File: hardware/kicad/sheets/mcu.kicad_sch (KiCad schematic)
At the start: 44 parts, among them J1 USB-C, J14 QWIIC, J5 DISPLAY, J6 NAV_SW, J7 AUX, SW1 RESET, SW2 BOOT, U1 ESP32-S3-WROOM-1U-N16R2, U4 SRV05-4

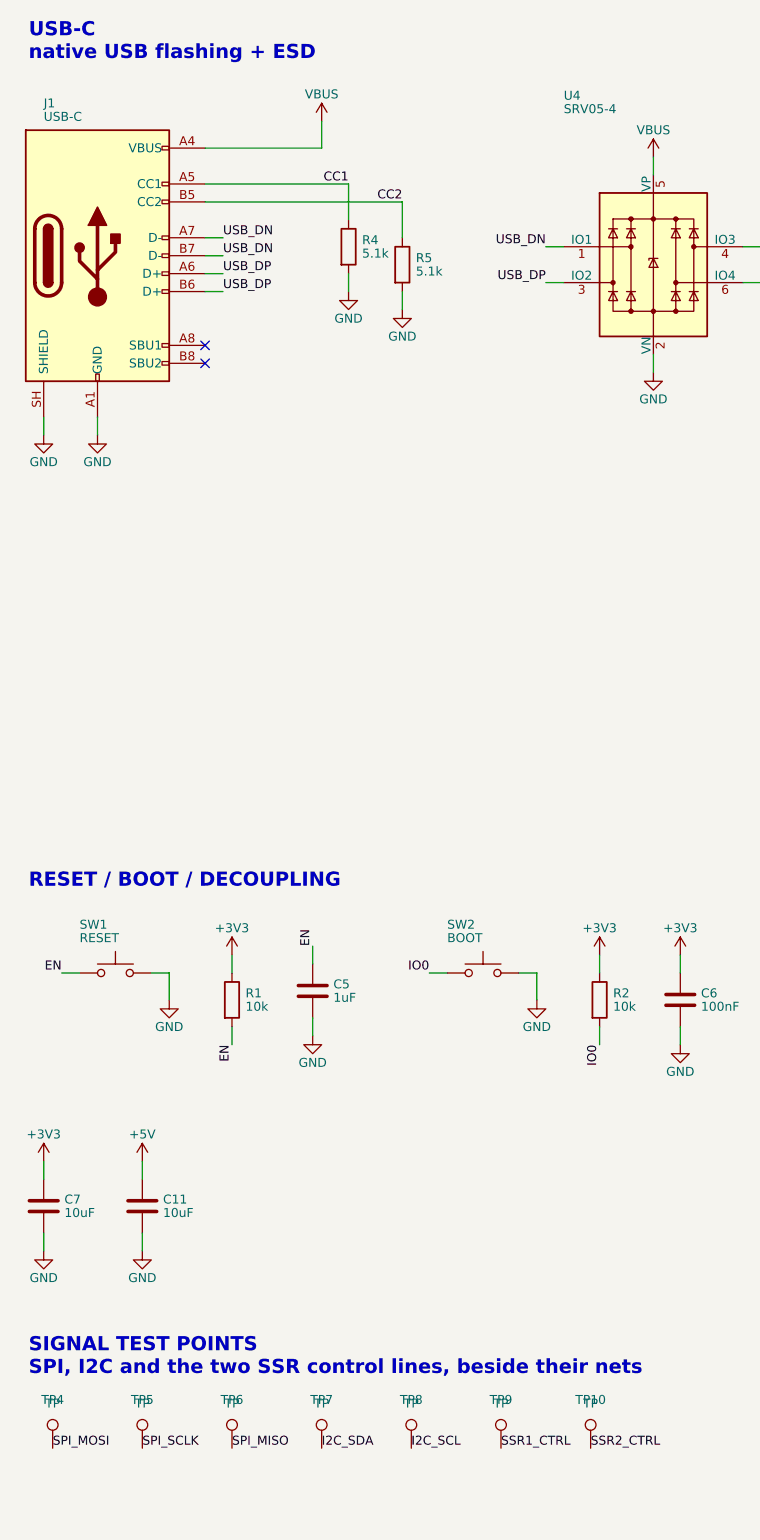
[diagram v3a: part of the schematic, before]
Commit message: hardware: flags at their sources, tri-state MAX31856, Q4 flipped, make erc
Second batch from SCHEMATIC-REVIEW-2026-10-22.md (findings 5, 7, 14, 15,
16 and the local half of 19).

PWR_FLAGs: the power sheet's parked corner is gone. Each flag now sits
where its rail is created - J2.1 (VIN), J2.2 (GND), Q8 source (VIN_P),
L1 output (BUCK_5V) and J1 pin A4 (VBUS, on the mcu sheet) - with the
value text shown on all of them.

MAX31856: U3 and U5 now use bisque:MAX31856 from the new project library
bisque.kicad_sym (registered in sym-lib-table), a copy of the KiCad
symbol with SDO typed tri-state, which is what the part does while CS is
high. The ERC exclusion that papered over the shared SPI_MISO is removed;
ERC is clean with no exclusions.

Q4 is mirrored so the high-side P-FET reads source-up to +5V and drain
down to SSR_EN. One Value string per LCSC part (C38/C44/C45 22uF/25V,
R11 100R 1%); C46 moved 5 mm right to clear the longer text. Every test
point's Value is its net name (TP1 "+3V3" ... TP12 "WDT_CT_P"), so the
board's Value fields, the JLC BOM and the schematic PDF regenerate.

make erc runs kicad-cli ERC at every severity and fails on any
violation; lib_symbol_mismatch, endpoint_off_grid and
same_local_global_label are promoted to errors in the project. It is not
part of pcb-check or CI on purpose.

Board: sync changed only Value fields (0 re-netted); gerbers differ by
timestamp only; DRC 0; full make pcb-check passes.

Co-Authored-By: Claude Fable 5.1 <noreply@anthropic.com>
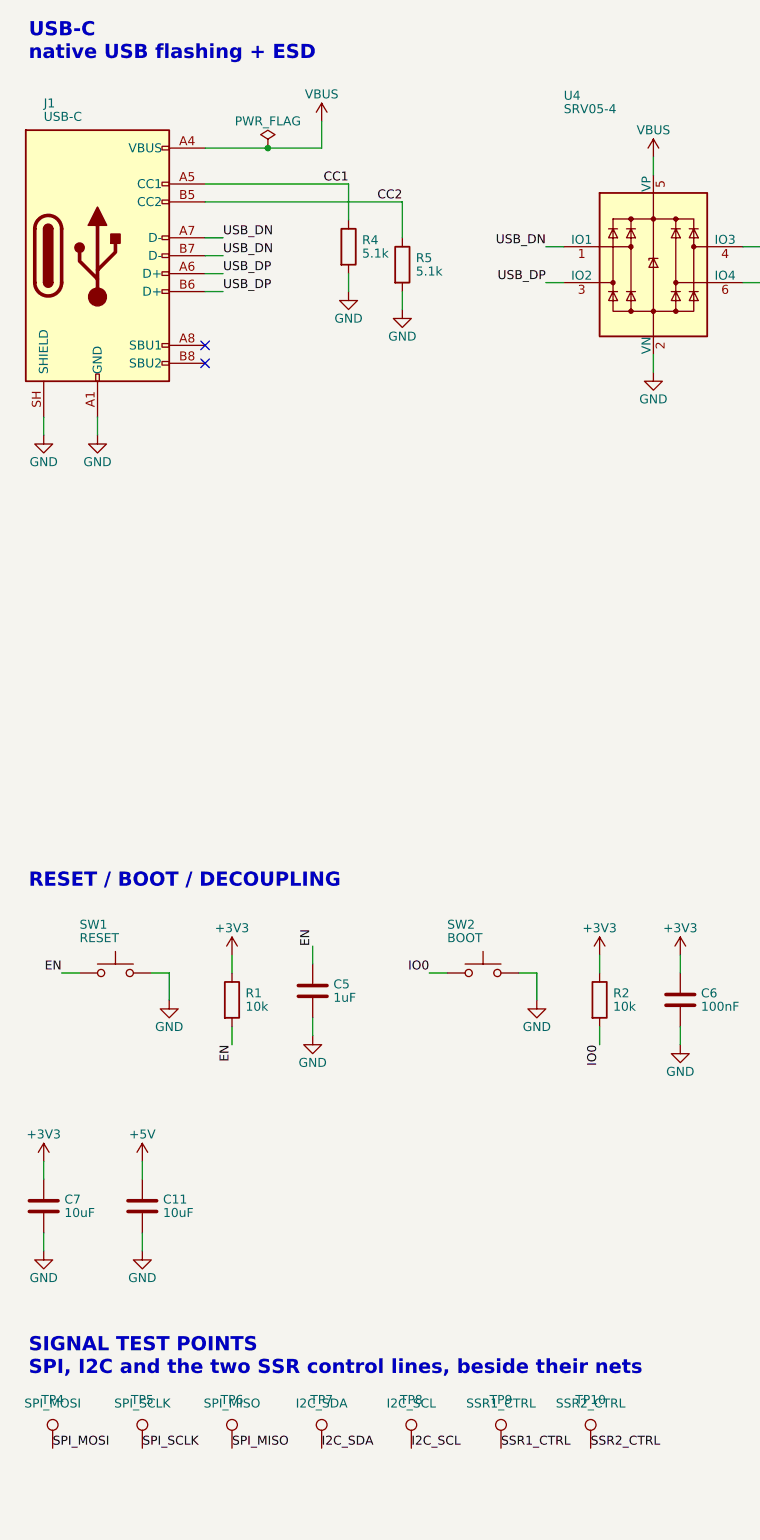
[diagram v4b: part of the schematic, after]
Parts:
- TP10: value TP -> SSR2_CTRL
- TP4: value TP -> SPI_MOSI
- TP5: value TP -> SPI_SCLK
- TP6: value TP -> SPI_MISO
- TP7: value TP -> I2C_SDA
- TP8: value TP -> I2C_SCL
- TP9: value TP -> SSR1_CTRL
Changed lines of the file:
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@@
 	)
 	(junction
+		(at 55.88 44.45)
+		(diameter 0)
+		(color 0 0 0 0)
+	)
+	(junction
 		(at 173.99 193.04)
 		(diameter 0)
@@
 			)
 		)
-		(property "Value" "TP"
+		(property "Value" "I2C_SCL"
 			(at 76.2 222.25 0)
 			(show_name no)
@@
 			)
 		)
-		(property "Value" "TP"
+		(property "Value" "SPI_MOSI"
 			(at 25.4 222.25 0)
 			(show_name no)
@@
 			)
 		)
-		(property "Value" "TP"
+		(property "Value" "SPI_SCLK"
 			(at 38.1 222.25 0)
 			(show_name no)
@@
 			)
 		)
-		(property "Value" "TP"
+		(property "Value" "SSR1_CTRL"
 			(at 88.9 222.25 0)
 			(show_name no)
@@
 			)
 		)
-		(property "Value" "TP"
+		(property "Value" "I2C_SDA"
 			(at 63.5 222.25 0)
 			(show_name no)
@@
 			)
 		)
-		(property "Value" "TP"
+		(property "Value" "SPI_MISO"
 			(at 50.8 222.25 0)
 			(show_name no)
@@
 			)
 		)
-		(property "Value" "TP"
+		(property "Value" "SSR2_CTRL"
 			(at 101.6 222.25 0)
 			(show_name no)
@@
 					(unit 1)
 				)
+			)
+		)
+	)
+	(symbol
+		(lib_id "power:PWR_FLAG")
+		(at 55.88 44.45 0)
+		(unit 1)
+		(body_style 1)
+		(exclude_from_sim no)
+		(in_bom yes)
+		(on_board yes)
+		(in_pos_files yes)
+		(dnp no)
+		(property "Reference" "#FLG06"
+			(at 55.88 42.545 0)
+			(hide yes)
+			(show_name no)
+			(do_not_autoplace no)
+			(effects
+				(font
+					(size 1.27 1.27)
+				)
+			)
+		)
+		(property "Value" "PWR_FLAG"
+			(at 55.88 40.64 0)
+			(show_name no)
+			(do_not_autoplace no)
+			(effects
+				(font
+					(size 1.27 1.27)
+				)
+			)
+		)
+		(property "Footprint" ""
+			(at 55.88 44.45 0)
+			(hide yes)
+			(show_name no)
+			(do_not_autoplace no)
+			(effects
+				(font
+					(size 1.27 1.27)
+				)
+			)
+		)
+		(property "Datasheet" ""
+			(at 55.88 44.45 0)
+			(hide yes)
+			(show_name no)
+			(do_not_autoplace no)
+			(effects
+				(font
+					(size 1.27 1.27)
+				)
+			)
+		)
+		(property "Description" "Special symbol for telling ERC where power comes from"
+			(at 55.88 44.45 0)
+			(hide yes)
+			(show_name no)
+			(do_not_autoplace no)
+			(effects
+				(font
+					(size 1.27 1.27)
+				)
+			)
+		)
+		(pin "1"
+		)
+		(instances
+			(project ""
+				(path "/1a47868a-bd78-50f4-b188-eb0464f4a928"
+					(reference "#FLG06")
+					(unit 1)
+				)

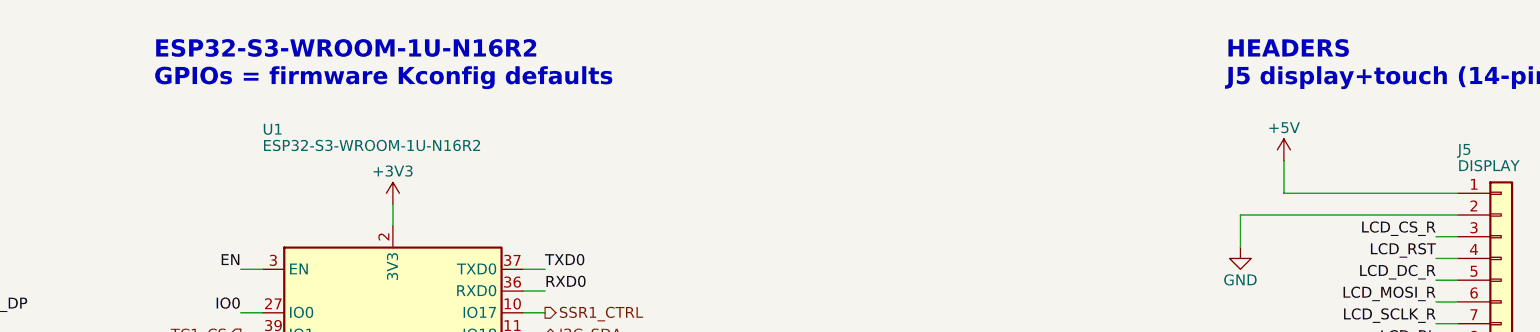
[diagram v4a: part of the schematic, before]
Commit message: hardware: honest symbols, real MPNs, U6 spares grounded, LCD_RST verified
Third batch from SCHEMATIC-REVIEW-2026-10-22.md (findings 6, 8, 11, 17,
18 and E1/E2).

Symbols: D8 is bisque:SMAJ30A (drawn as a zener with its cathode on the
rail, since the fitted TVS is unidirectional), Q5-Q7 are bisque:CJ2310
and U2 is bisque:TLV1117LV33, each a flattened copy of the stock symbol
with the fitted part's name, description and LCSC-hosted datasheet, so
no pin or wire moved. The stock D_TVS, 2N7002 and TLV1117-33 embeds are
gone from the sheets.

Sourcing: every one of the 160 assembled symbols now carries MPN (the
manufacturer's part number, from LCSC's product record for its C-number),
Manufacturer and Datasheet (LCSC's hosted PDF) beside LCSC. check_mpn.py
keeps LCSC tied to gen_jlc.LCSC and requires the other two to be present
and MPN not to be a bare C-number.

Drawing: J11's IN1_RAW/IN2_RAW labels read along their own wires instead
of across the connector; U6's unused Darlington inputs I4-I7 are tied to
GND (the board's F.Cu pour already covers them - 4 pads re-netted, 0
unconnected, DRC 0); the root notes record the retired designators and
the LCD_RST finding (the MSP4021's own schematic shows no pull-up on
RESET, so GPIO46 does not block download mode); the mcu sheet notes that
GPIO35/36 rule out R8 (octal PSRAM) modules.

The datasheet manifest maps the shared 22uF/25V sheet to the unified
value and exempts the test points' net-name values. Full make pcb-check
passes; gerbers differ by timestamp and the re-filled GND pour; 3D
renders refreshed.

Co-Authored-By: Claude Fable 5.1 <noreply@anthropic.com>
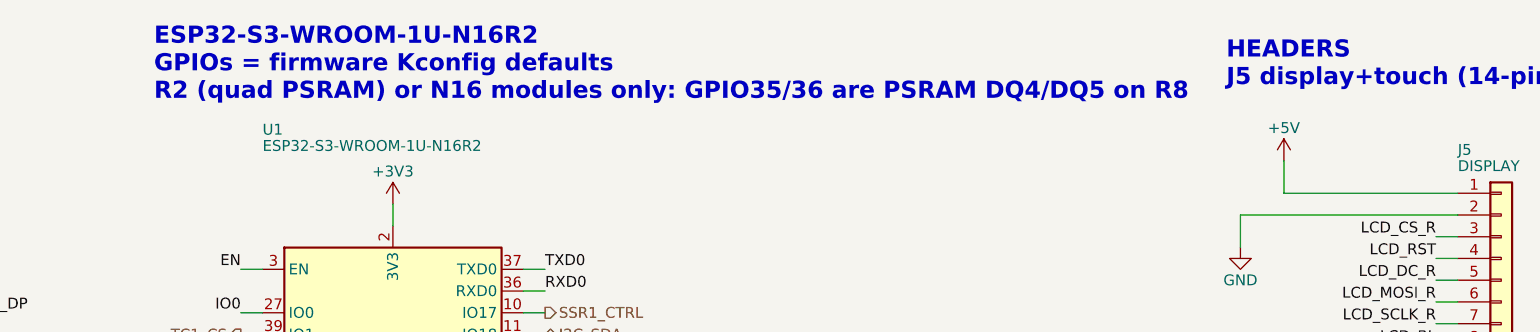
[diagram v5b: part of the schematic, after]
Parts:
- C10, C6: MPN C49678 -> CC0805KRX7R9BB104; Manufacturer (none) -> YAGEO
- C11, C7: MPN C15850 -> CL21A106KAYNNNE; Manufacturer (none) -> Samsung Electro-Mechanics
- C5: MPN C28323 -> CL21B105KBFNNNE; Manufacturer (none) -> Samsung Electro-Mechanics
- D3: MPN C81598 -> 1N4148W; Manufacturer (none) -> ST(Semtech)
- J1: MPN C165948 -> TYPE-C-31-M-12; Manufacturer (none) -> Korean Hroparts Elec
- J14: MPN C160404 -> SM04B-SRSS-TB(LF)(SN); Manufacturer (none) -> JST
- J5: MPN C17701004 -> XD-2510-14A; Manufacturer (none) -> chxunda
- J6: MPN C239381 -> A2547WV-6P; Manufacturer (none) -> CJT(Changjiang Connectors)
- J7: MPN C240822 -> 22272081; Manufacturer (none) -> MOLEX
- LED1: MPN C2761795 -> WS2812B-B/T; Manufacturer (none) -> Worldsemi
- R1, R2, R50, R51, R52, R53: MPN C17414 -> 0805W8F1002T5E; Manufacturer (none) -> UNI-ROYAL
- R3: MPN C17630 -> 0805W8F3300T5E; Manufacturer (none) -> UNI-ROYAL
- R39, R40, R41, R42, R43, R54, R55, R56, R57, R58: MPN C17634 -> 0805W8F330JT5E; Manufacturer (none) -> UNI-ROYAL
- R4, R5: MPN C27834 -> 0805W8F5101T5E; Manufacturer (none) -> UNI-ROYAL
- R44, R45: MPN C17673 -> 0805W8F4701T5E; Manufacturer (none) -> UNI-ROYAL
- SW1, SW2: MPN C318884 -> TS-1187A-B-A-B; Manufacturer (none) -> XKB Connection
- U1: MPN C3013945 -> ESP32-S3-WROOM-1U-N16R2; Manufacturer (none) -> ESPRESSIF
- U4: MPN C7420376 -> SRV05-4; Manufacturer (none) -> R+O
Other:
- note added: "ESP32-S3-WROOM-1U-N16R2 GPIOs = firmware Kconfig defaults R2 (quad PSRAM) or N16 modules only: GPIO35/36 are PSRAM DQ4/DQ5 on R8"
- note removed: "ESP32-S3-WROOM-1U-N16R2 GPIOs = firmware Kconfig defaults"
